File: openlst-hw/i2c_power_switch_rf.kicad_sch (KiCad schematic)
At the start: 7 parts, among them U10 MCP23008T-E/SS, U11 INA226AIDGSR

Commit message: EPS AVI SCI SCIwoSwitches RF AUX all updated to use RNs. BOMs completed
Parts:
- R20: renamed from R27; Part Number RC0402FR-0747KL -> RC0402FR-07100KL
- renumbered C48 to C46, C49 to C47, C50 to C48, R28 to R21, U11 to U10, U10 to U9
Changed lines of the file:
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@@
 		(dnp yes)
 		(fields_autoplaced yes)
-		(property "Reference" "C50"
+		(property "Reference" "C48"
 			(at 52.07 118.7449 0)
 			(effects
@@
 			(project "openlst-hw"
 				(path "/a863a5ec-a5d4-4f54-be53-e8c01d5e3ac4/53f12969-e593-459a-9671-cc23a5a9aea0/158b6ecf-5b25-4ecb-8b1c-83236ab855da"
-					(reference "C50")
+					(reference "C48")
 					(unit 1)
 				)
@@
 		(dnp no)
 		(fields_autoplaced yes)
-		(property "Reference" "C48"
+		(property "Reference" "C46"
 			(at 121.285 40.0049 0)
 			(effects
@@
 			(project "openlst-hw"
 				(path "/a863a5ec-a5d4-4f54-be53-e8c01d5e3ac4/53f12969-e593-459a-9671-cc23a5a9aea0/158b6ecf-5b25-4ecb-8b1c-83236ab855da"
-					(reference "C48")
+					(reference "C46")
 					(unit 1)
 				)
@@
 		(on_board yes)
 		(dnp no)
-		(property "Reference" "R27"
+		(property "Reference" "R20"
 			(at 104.775 40.005 0)
 			(effects
@@
 			)
 		)
-		(property "Part Number" "RC0402FR-0747KL"
+		(property "Part Number" "RC0402FR-07100KL"
 			(at 111.76 41.275 0)
 			(effects
@@
 			(project "openlst-hw"
 				(path "/a863a5ec-a5d4-4f54-be53-e8c01d5e3ac4/53f12969-e593-459a-9671-cc23a5a9aea0/158b6ecf-5b25-4ecb-8b1c-83236ab855da"
-					(reference "R27")
+					(reference "R20")
 					(unit 1)
 				)
@@
 		(dnp no)
 		(fields_autoplaced yes)
-		(property "Reference" "U11"
+		(property "Reference" "U10"
 			(at 73.025 73.025 0)
 			(effects
@@
 			(project "openlst-hw"
 				(path "/a863a5ec-a5d4-4f54-be53-e8c01d5e3ac4/53f12969-e593-459a-9671-cc23a5a9aea0/158b6ecf-5b25-4ecb-8b1c-83236ab855da"
-					(reference "U11")
+					(reference "U10")
 					(unit 1)
 				)
@@
 		(on_board yes)
 		(dnp no)
-		(property "Reference" "R28"
+		(property "Reference" "R21"
 			(at 50.165 95.885 0)
 			(effects
@@
 			(project "openlst-hw"
 				(path "/a863a5ec-a5d4-4f54-be53-e8c01d5e3ac4/53f12969-e593-459a-9671-cc23a5a9aea0/158b6ecf-5b25-4ecb-8b1c-83236ab855da"
-					(reference "R28")
+					(reference "R21")
 					(unit 1)
 				)
@@
 		(dnp no)
 		(fields_autoplaced yes)
-		(property "Reference" "U10"
+		(property "Reference" "U9"
 			(at 80.01 25.4 0)
 			(effects
@@
 			(project "openlst-hw"
 				(path "/a863a5ec-a5d4-4f54-be53-e8c01d5e3ac4/53f12969-e593-459a-9671-cc23a5a9aea0/158b6ecf-5b25-4ecb-8b1c-83236ab855da"
-					(reference "U10")
+					(reference "U9")
 					(unit 1)
 				)
@@
 		(dnp no)
 		(fields_autoplaced yes)
-		(property "Reference" "C49"
+		(property "Reference" "C47"
 			(at 101.6 83.1849 0)
 			(effects
@@
 			(project "openlst-hw"
 				(path "/a863a5ec-a5d4-4f54-be53-e8c01d5e3ac4/53f12969-e593-459a-9671-cc23a5a9aea0/158b6ecf-5b25-4ecb-8b1c-83236ab855da"
-					(reference "C49")
-					(unit 1)
-				)
+					(reference "C47")
+					(unit 1)
+				)

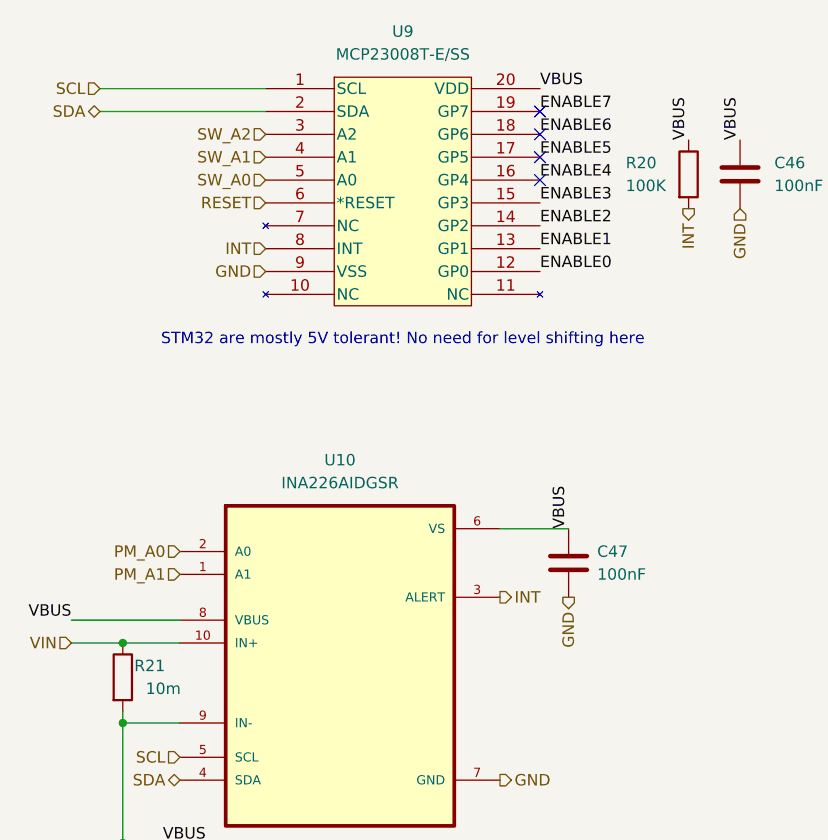
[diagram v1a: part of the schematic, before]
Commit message: move SPI CS pullups to outer schema to combine multiple with RNs
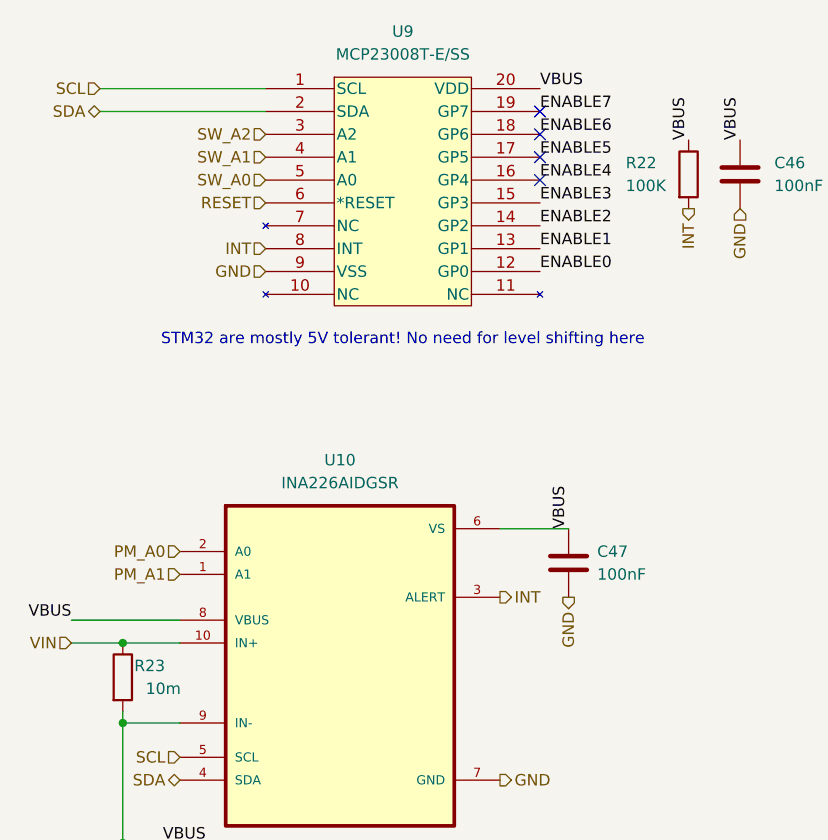
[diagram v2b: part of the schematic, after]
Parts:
- renumbered R20 to R22, R21 to R23
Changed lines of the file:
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@@
 		(on_board yes)
 		(dnp no)
-		(property "Reference" "R20"
+		(property "Reference" "R22"
 			(at 104.775 40.005 0)
 			(effects
@@
 			(project "openlst-hw"
 				(path "/a863a5ec-a5d4-4f54-be53-e8c01d5e3ac4/53f12969-e593-459a-9671-cc23a5a9aea0/158b6ecf-5b25-4ecb-8b1c-83236ab855da"
-					(reference "R20")
+					(reference "R22")
 					(unit 1)
 				)
@@
 		(on_board yes)
 		(dnp no)
-		(property "Reference" "R21"
+		(property "Reference" "R23"
 			(at 50.165 95.885 0)
 			(effects
@@
 			(project "openlst-hw"
 				(path "/a863a5ec-a5d4-4f54-be53-e8c01d5e3ac4/53f12969-e593-459a-9671-cc23a5a9aea0/158b6ecf-5b25-4ecb-8b1c-83236ab855da"
-					(reference "R21")
-					(unit 1)
-				)
+					(reference "R23")
+					(unit 1)
+				)
